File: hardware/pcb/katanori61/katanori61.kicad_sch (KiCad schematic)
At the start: 53 parts, among them J1 XIAO RISER, J10 BAT (JST-PH), J13 USB-C, J2 OLED, J4 SPK IN, J5 SPK OUT, J6 BTN2, J7 REED+TOGGLE, K31 G6S-2F DC5, Q1 MMUN2133LT1G, Q31 SS8050, U1 TPS61090RSAR, U2 MCP73871-2CCI/ML, U3 INA226AIDGSR, U4 AS5600-ASOM

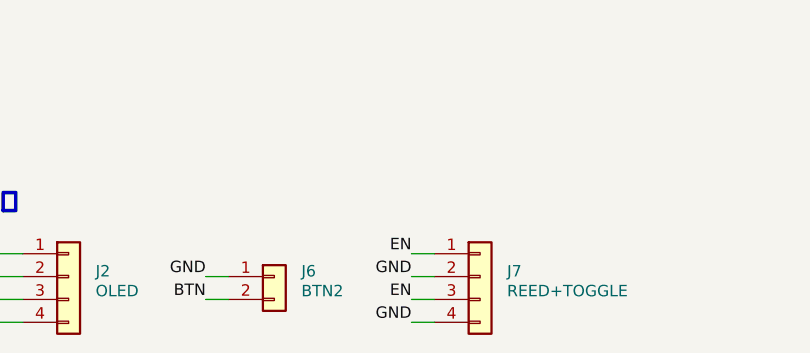
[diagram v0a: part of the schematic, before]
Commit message: 会話ボタンの口（J6）を板から外す（🔒 ユーザー 2026-09-14）
口は 4 つ（スピーカー IN・OUT・リード＋トグル・電池）になった。配線し直して
DRC のエラー 0・未接続 0。ガーバーと部品表も出し直した（実装は 29 種類 46 個で変わらず、
自分で付けるのが 7 → 6 個）。

⚠ BTN（XIAO の D2）は板の上では J1 の 6 番だけになった。会話ボタンの行き先は未決。
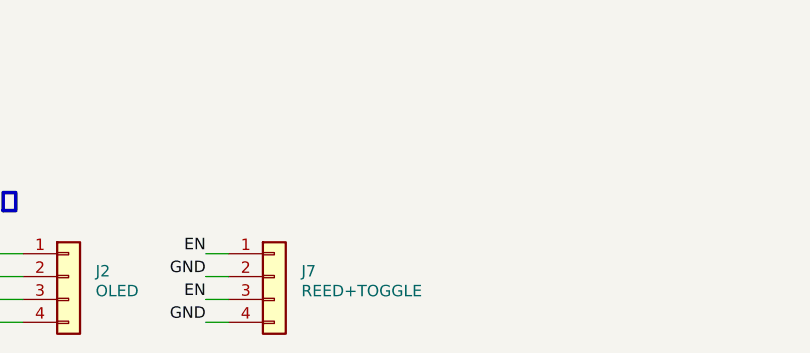
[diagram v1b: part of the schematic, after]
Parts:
- removed J7: REED+TOGGLE, Connector_JST:JST_PH_B4B-PH-K_1x04_P2.00mm_Vertical, symbol Connector_Generic:Conn_01x04
- J7: renamed from J6; value BTN2 -> REED+TOGGLE; footprint Connector_JST:JST_PH_S2B-PH-K_1x02_P2.00mm_Horizontal -> Connector_JST:JST_PH_B4B-PH-K_1x04_P2.00mm_Vertical; symbol Connector_Generic:Conn_01x02 -> Connector_Generic:Conn_01x04; Note 筐体の会話ボタンへ 2 本 -> 1 EN・2 GND → リード ／ 3 EN・4 GND → マスタートグル（縦の口・上から挿す）
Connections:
- net BTN: no longer J7.2 (Pin_2)
- net EN: now also J7.1 (Pin_1), J7.3 (Pin_3)
- net GND: now also J7.2 (Pin_2), J7.4 (Pin_4); no longer J7.1 (Pin_1)
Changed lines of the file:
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@@
 	)
 	(symbol
-		(lib_id "Connector_Generic:Conn_01x02")
+		(lib_id "Connector_Generic:Conn_01x04")
 		(at 109.22 243.84 0)
 		(unit 1)
@@
 		(on_board yes)
 		(dnp no)
-		(property "Reference" "J6"
+		(property "Reference" "J7"
 			(at 112.22 243.24 0)
 			(effects
@@
 			)
 		)
-		(property "Value" "BTN2"
+		(property "Value" "REED+TOGGLE"
 			(at 112.22 245.44 0)
 			(effects
@@
 			)
 		)
-		(property "Footprint" "Connector_JST:JST_PH_S2B-PH-K_1x02_P2.00mm_Horizontal"
+		(property "Footprint" "Connector_JST:JST_PH_B4B-PH-K_1x04_P2.00mm_Vertical"
 			(at 109.22 243.84 0)
 			(effects
@@
 			)
 		)
-		(property "Note" "筐体の会話ボタンへ 2 本"
+		(property "Note" "1 EN・2 GND → リード ／ 3 EN・4 GND → マスタートグル（縦の口・上から挿す）"
 			(at 109.22 243.84 0)
 			(effects
@@
 		(pin "2"
 		)
+		(pin "3"
+		)
+		(pin "4"
+		)
 		(instances
 			(project "katanori61"
 				(path "/377120ba-3fb3-530c-9f35-c36cf0274025"
-					(reference "J6")
+					(reference "J7")
 					(unit 1)
 				)
 			)
+		)
+	)
+	(wire
+		(pts
+			(xy 104.14 241.30)
+			(xy 101.60 241.30)
+		)
+		(stroke
+			(width 0)
+			(type default)
+		)
+	)
+	(label "EN"
+		(at 101.60 241.30 180)
+		(effects
+			(font
+				(size 1.27 1.27)
+			)
+			(justify right bottom)
 		)
 	)
@@
 		)
 	)
-	(label "BTN"
+	(label "EN"
 		(at 101.60 246.38 180)
-		(effects
-			(font
-				(size 1.27 1.27)
-			)
-			(justify right bottom)
-		)
-	)
-	(symbol
-		(lib_id "Connector_Generic:Conn_01x04")
-		(at 132.08 243.84 0)
-		(unit 1)
-		(exclude_from_sim no)
-		(in_bom yes)
-		(on_board yes)
-		(dnp no)
-		(property "Reference" "J7"
-			(at 135.08 243.24 0)
-			(effects
-				(font
-					(size 1.27 1.27)
-				)
-				(justify left)
-			)
-		)
-		(property "Value" "REED+TOGGLE"
-			(at 135.08 245.44 0)
-			(effects
-				(font
-					(size 1.27 1.27)
-				)
-				(justify left)
-			)
-		)
-		(property "Footprint" "Connector_JST:JST_PH_B4B-PH-K_1x04_P2.00mm_Vertical"
-			(at 132.08 243.84 0)
-			(effects
-				(font
-					(size 1.27 1.27)
-				)
-				(hide yes)
-			)
-		)
-		(property "Datasheet" ""
-			(at 132.08 243.84 0)
-			(effects
-				(font
-					(size 1.27 1.27)
-				)
-				(hide yes)
-			)
-		)
-		(property "Note" "1 EN・2 GND → リード ／ 3 EN・4 GND → マスタートグル（縦の口・上から挿す）"
-			(at 132.08 243.84 0)
-			(effects
-				(font
-					(size 1.27 1.27)
-				)
-				(hide yes)
-			)
-		)
-		(pin "1"
-		)
-		(pin "2"
-		)
-		(pin "3"
-		)
-		(pin "4"
-		)
-		(instances
-			(project "katanori61"
-				(path "/377120ba-3fb3-530c-9f35-c36cf0274025"
-					(reference "J7")
-					(unit 1)
-				)
-			)
-		)
-	)
-	(wire
-		(pts
-			(xy 127.00 241.30)
-			(xy 124.46 241.30)
-		)
-		(stroke
-			(width 0)
-			(type default)
-		)
-	)
-	(label "EN"
-		(at 124.46 241.30 180)
 		(effects
 			(font
@@
 	(wire
 		(pts
-			(xy 127.00 243.84)
-			(xy 124.46 243.84)
+			(xy 104.14 248.92)
+			(xy 101.60 248.92)
 		)
 		(stroke
@@
 	)
 	(label "GND"
-		(at 124.46 243.84 180)
+		(at 101.60 248.92 180)
 		(effects
 			(font
-				(size 1.27 1.27)
-			)
-			(justify right bottom)
-		)
-	)
-	(wire
-		(pts
-			(xy 127.00 246.38)
-			(xy 124.46 246.38)
-		)
-		(stroke
-			(width 0)
-			(type default)
-		)
-	)
-	(label "EN"
-		(at 124.46 246.38 180)
-		(effects
-			(font
-				(size 1.27 1.27)
-			)
-			(justify right bottom)
-		)
-	)
-	(wire
-		(pts
-			(xy 127.00 248.92)
-			(xy 124.46 248.92)
-		)
-		(stroke
-			(width 0)
-			(type default)
-		)
-	)
-	(label "GND"
-		(at 124.46 248.92 180)
-		(effects
-			(font

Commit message: 会話ボタンの口（J6）を戻す（外したのは伝言の読み違い）
🔒 ユーザー 2026-09-14「会話ボタンを基板に付ける必要はないと言ったんであって、線は必要でしょ。
天板の会話ボタンはあるんだし」＝ 押しボタンを板に載せないだけで、線を受ける口は要る。

枠も向きも外す前と同じ（板の座標 X 14.05〜20.95・Y 22.70〜31.30・口は −Y）。
板の部品 53・線が出る口 5 つ・自分で付ける 7 個に戻った。DRC のエラー 0・未接続 0。
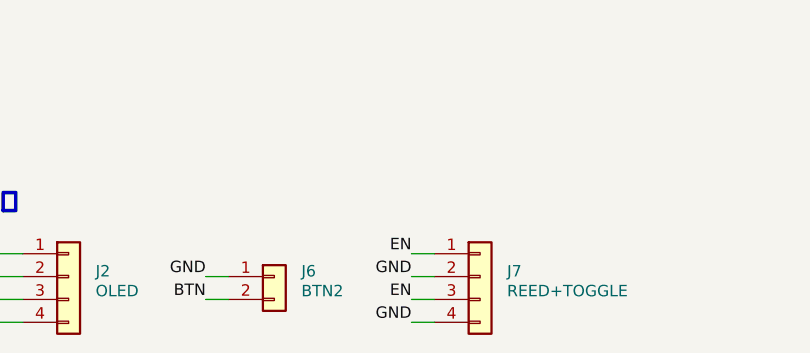
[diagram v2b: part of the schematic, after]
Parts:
- added J7: REED+TOGGLE, Connector_JST:JST_PH_B4B-PH-K_1x04_P2.00mm_Vertical, symbol Connector_Generic:Conn_01x04
- J6: renamed from J7; value REED+TOGGLE -> BTN2; footprint Connector_JST:JST_PH_B4B-PH-K_1x04_P2.00mm_Vertical -> Connector_JST:JST_PH_S2B-PH-K_1x02_P2.00mm_Horizontal; symbol Connector_Generic:Conn_01x04 -> Connector_Generic:Conn_01x02; Note 1 EN・2 GND → リード ／ 3 EN・4 GND → マスタートグル（縦の口・上から挿す） -> 天板の会話ボタンへ 2 本
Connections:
- net BTN: now also J6.2 (Pin_2)
- net EN: now also J7.1 (Pin_1), J7.3 (Pin_3); no longer J6.1 (Pin_1), J6.3 (Pin_3)
- net GND: now also J6.1 (Pin_1), J7.2 (Pin_2), J7.4 (Pin_4); no longer J6.2 (Pin_2), J6.4 (Pin_4)
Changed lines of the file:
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@@
 	)
 	(symbol
-		(lib_id "Connector_Generic:Conn_01x04")
+		(lib_id "Connector_Generic:Conn_01x02")
 		(at 109.22 243.84 0)
 		(unit 1)
@@
 		(on_board yes)
 		(dnp no)
-		(property "Reference" "J7"
+		(property "Reference" "J6"
 			(at 112.22 243.24 0)
 			(effects
@@
 			)
 		)
-		(property "Value" "REED+TOGGLE"
+		(property "Value" "BTN2"
 			(at 112.22 245.44 0)
 			(effects
@@
 			)
 		)
-		(property "Footprint" "Connector_JST:JST_PH_B4B-PH-K_1x04_P2.00mm_Vertical"
+		(property "Footprint" "Connector_JST:JST_PH_S2B-PH-K_1x02_P2.00mm_Horizontal"
 			(at 109.22 243.84 0)
 			(effects
@@
 			)
 		)
+		(property "Note" "天板の会話ボタンへ 2 本"
+			(at 109.22 243.84 0)
+			(effects
+				(font
+					(size 1.27 1.27)
+				)
+				(hide yes)
+			)
+		)
+		(pin "1"
+		)
+		(pin "2"
+		)
+		(instances
+			(project "katanori61"
+				(path "/377120ba-3fb3-530c-9f35-c36cf0274025"
+					(reference "J6")
+					(unit 1)
+				)
+			)
+		)
+	)
+	(wire
+		(pts
+			(xy 104.14 243.84)
+			(xy 101.60 243.84)
+		)
+		(stroke
+			(width 0)
+			(type default)
+		)
+	)
+	(label "GND"
+		(at 101.60 243.84 180)
+		(effects
+			(font
+				(size 1.27 1.27)
+			)
+			(justify right bottom)
+		)
+	)
+	(wire
+		(pts
+			(xy 104.14 246.38)
+			(xy 101.60 246.38)
+		)
+		(stroke
+			(width 0)
+			(type default)
+		)
+	)
+	(label "BTN"
+		(at 101.60 246.38 180)
+		(effects
+			(font
+				(size 1.27 1.27)
+			)
+			(justify right bottom)
+		)
+	)
+	(symbol
+		(lib_id "Connector_Generic:Conn_01x04")
+		(at 132.08 243.84 0)
+		(unit 1)
+		(exclude_from_sim no)
+		(in_bom yes)
+		(on_board yes)
+		(dnp no)
+		(property "Reference" "J7"
+			(at 135.08 243.24 0)
+			(effects
+				(font
+					(size 1.27 1.27)
+				)
+				(justify left)
+			)
+		)
+		(property "Value" "REED+TOGGLE"
+			(at 135.08 245.44 0)
+			(effects
+				(font
+					(size 1.27 1.27)
+				)
+				(justify left)
+			)
+		)
+		(property "Footprint" "Connector_JST:JST_PH_B4B-PH-K_1x04_P2.00mm_Vertical"
+			(at 132.08 243.84 0)
+			(effects
+				(font
+					(size 1.27 1.27)
+				)
+				(hide yes)
+			)
+		)
+		(property "Datasheet" ""
+			(at 132.08 243.84 0)
+			(effects
+				(font
+					(size 1.27 1.27)
+				)
+				(hide yes)
+			)
+		)
 		(property "Note" "1 EN・2 GND → リード ／ 3 EN・4 GND → マスタートグル（縦の口・上から挿す）"
-			(at 109.22 243.84 0)
+			(at 132.08 243.84 0)
 			(effects
 				(font
@@
 	(wire
 		(pts
-			(xy 104.14 241.30)
-			(xy 101.60 241.30)
+			(xy 127.00 241.30)
+			(xy 124.46 241.30)
 		)
 		(stroke
@@
 	)
 	(label "EN"
-		(at 101.60 241.30 180)
-		(effects
-			(font
-				(size 1.27 1.27)
-			)
-			(justify right bottom)
-		)
-	)
-	(wire
-		(pts
-			(xy 104.14 243.84)
-			(xy 101.60 243.84)
+		(at 124.46 241.30 180)
+		(effects
+			(font
+				(size 1.27 1.27)
+			)
+			(justify right bottom)
+		)
+	)
+	(wire
+		(pts
+			(xy 127.00 243.84)
+			(xy 124.46 243.84)
 		)
 		(stroke
@@
 	)
 	(label "GND"
-		(at 101.60 243.84 180)
-		(effects
-			(font
-				(size 1.27 1.27)
-			)
-			(justify right bottom)
-		)
-	)
-	(wire
-		(pts
-			(xy 104.14 246.38)
-			(xy 101.60 246.38)
+		(at 124.46 243.84 180)
+		(effects
+			(font
+				(size 1.27 1.27)
+			)
+			(justify right bottom)
+		)
+	)
+	(wire
+		(pts
+			(xy 127.00 246.38)
+			(xy 124.46 246.38)
 		)
 		(stroke
@@
 	)
 	(label "EN"
-		(at 101.60 246.38 180)
-		(effects
-			(font
-				(size 1.27 1.27)
-			)
-			(justify right bottom)
-		)
-	)
-	(wire
-		(pts
-			(xy 104.14 248.92)
-			(xy 101.60 248.92)
+		(at 124.46 246.38 180)
+		(effects
+			(font
+				(size 1.27 1.27)
+			)
+			(justify right bottom)
+		)
+	)
+	(wire
+		(pts
+			(xy 127.00 248.92)
+			(xy 124.46 248.92)
 		)
 		(stroke
@@
 	)
 	(label "GND"
-		(at 101.60 248.92 180)
-		(effects
-			(font
+		(at 124.46 248.92 180)
+		(effects
+			(font

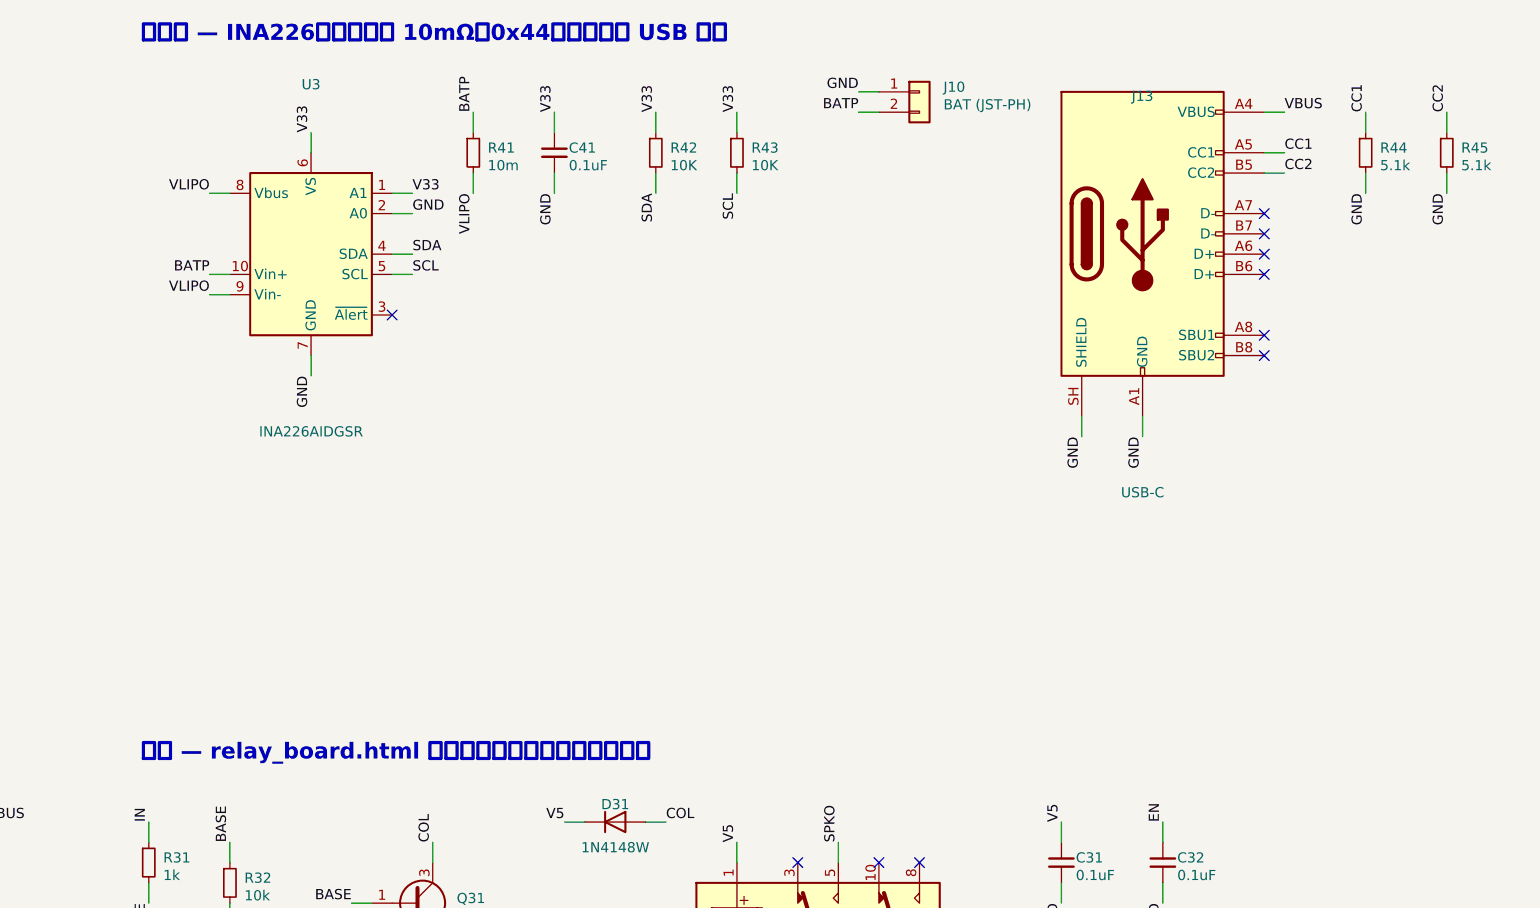
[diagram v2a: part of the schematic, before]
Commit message: pcb v6.1: J10 を縦の B2B-PH-K へ・逆接保護の MOSFET を追加・取付穴の移動と欠きの全廃に追随
筐体側の 2026-09-16 夕の作り替え（電池のケーシング・床から立つ左後ろの柱）に合わせて、
基板を出し直した。DRC エラー 0・未接続 0・回路図との食い違い 0。

■ J10（電池の口）を縦へ
🔒 ユーザー「ケーシング作ったから垂直のがいい。結局一番穴は小さくなる」。
サイド型 S2B-PH-K（背 4.8・横出し）→ トップ型 B2B-PH-K を板の裏に下向き。左の帯 → 右の帯。
・天板の窓が 12.7 × 7.9（100.3mm2）→ 8.11 × 5.91（47.9mm2）。挿しても平面の外形が広がらない
  （ハウジング PHR-2 5.8 × 4.5 が胴 5.9 × 4.5 の中に収まる。ePH.pdf 3 ページ）
・J10 は板の裏でも、はんだ足 2 本は表へ突き抜ける。その足を J4 の胴（板 y 〜14.30）と
  J4 に挿さったプラグ（〜16.30）の外へ出す必要があり、USB-C のシェルの足（20.63〜）との
  あいだが 4.33 しか無いのでパッドを Y 並び → X 並びへ回した
・その結果、極性の言い方が「手前／奥」から「左／右」へ変わった（右 77.45 が GND・左 75.45 が VBAT+）。
  ネットの割り当て（1 番 = GND・2 番 = +）は変えていない

■ 逆接保護の P-ch MOSFET（Q2）
🔒 ユーザー「MOSFET 一つ入れましょ」。J10 の 2 番とシャント R41 のあいだへ。
・AO3401A（LCSC C15127・JLCPCB Basic・Vgs(th) 900mV・RDS(on) 60mΩ@4.5V / 85mΩ@2.5V）
  ＋ ゲートの 100kΩ（R46 は R17 と同じ品なので部品の種類は増えない）
・ドレイン(3) = 電池側 BATRAW / ソース(2) = 負荷側 BATP / ゲート(1) = 100kΩ で GND。
  逆に繋ぐとボディダイオードが逆方向・Vgs = 0 でチャネルも閉じたまま → 電流が流れない
・保護の外に残るのは BATRAW の線と Q2 のドレインだけ。2026-09-11 に焼けた INA226 は
  入力も電源も内側にある。逆接の症状は「何も起きない」になる
・J10 の横は J4 のプラグの逃げと USB-C に挟まれて 2.78 しか無く SOT-23 が入らないので
  シャントの隣に置いた。電池の電流はもともと板を横断しているので経路は伸びない

■ 筐体の作り替えへの追随
・取付穴 4 点: (4.0, 3.5) (72.5, 3.5) (2.834, 33.9942) (79.354, 34.9)。4 点とも使う
  （上から 3 本・下から 1 本）。旧の後ろ 2 点 (10.0, 33.4) (72.5, 33.4) から移動
・板の欠きを全廃。残るのは後ろのレールの逃げ（板 X 0〜1.694・Y 37.1〜37.4）だけ。
  幅はレール 1.2 + 板を右へ 0.8 滑らせる分。銅が 41mm2 戻った
・板の裏は両材料とも Z 12.0（BAT_CASE 6.0 がレジンにも入った）

■ 検査の道具の直し（どれも見落としを実際に出したもの）
・gen_pcb: 枠の重なりを面ごとに。表と裏を 1 枚の紙として見ていて、板を挟んで別の側に居る物を
  重なりと呼んでいた。別の面どうしは「板を貫く足が相手の胴に入っていないか」で見る
・gen_pcb: courtyard() に key="Fab" を足した。courtyard は置き場所の予約で物の形ではない
・gen_pcb: プラグの通り道の検査が、裏の部品の足を見ていなかった。J10 の足が J4 のプラグの
  真下に入るのを筐体側の hit_wires が先に見つけた
・gen_pcb: 押し離しも面ごとに（表と裏で押し合って収束しなかった）
・gen_pcb: PLUG_BODY 3.1 → 1.5。3.1 は導出が間違っていた（SMT の図の (9.6) から
  トップ型の背 6.0 を引いていた。正はサイド型の奥行き 7.6 を引いて 2.0 = courtyard から 1.5）
  押し離しの予約だけは 3.1 のまま（PLUG_KEEP・置き方の手加減で検査の値ではない）
・route.py --incremental: 「φ0.59 以上は縫いのビア」として自動配線のビア（φ0.8）まで
  種から落としていた。多層をまたぐネットが切れて未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
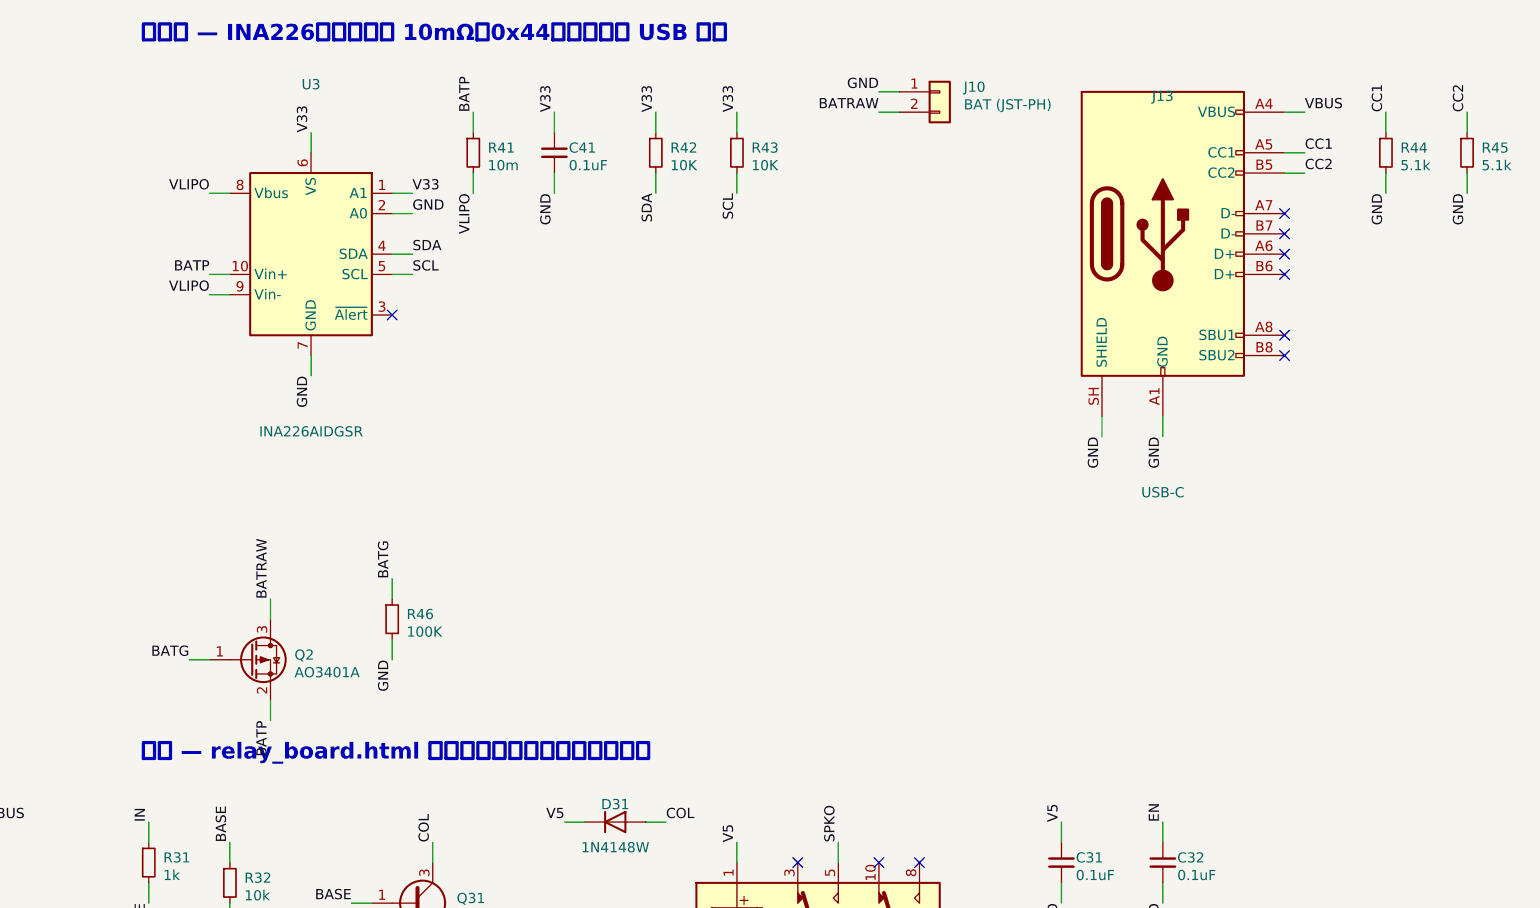
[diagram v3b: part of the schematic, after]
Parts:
- removed Q31: SS8050, Package_TO_SOT_SMD:SOT-23, symbol Transistor_BJT:MMBT3904
- removed R32: 10k, Resistor_SMD:R_0805_2012Metric, symbol Device:R_Small
- added D31: 1N4148W, Diode_SMD:D_SOD-123, symbol Diode:1N4148W
- added K31: G6S-2F DC5, Relay_SMD:Relay_DPDT_Omron_G6S-2F, symbol Relay:G6S-2
- added R31: 1k, Resistor_SMD:R_0805_2012Metric, symbol Device:R_Small
- added R46: 100K, Resistor_SMD:R_0805_2012Metric, symbol Device:R_Small
- J10: footprint Connector_JST:JST_PH_S2B-PH-K_1x02_P2.00mm_Horizontal -> Connector_JST:JST_PH_B2B-PH-K_1x02_P2.00mm_Vertical; Note 🔴 1 番が −・2 番が +（PowerBoost B1 の並び）。v6.1 は板の裏に横出し（🔒 ユーザー 202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 -> 🔴 1 番が −・2 番が ＋（PowerBoost B1 の並び。⭐ 2026-09-16 夕から 2 番のネットは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
- Q2: renamed from R31; value 1k -> AO3401A; footprint Resistor_SMD:R_0805_2012Metric -> Package_TO_SOT_SMD:SOT-23; symbol Device:R_Small -> Transistor_FET:Q_PMOS_GSD; LCSC C17513 -> C15127; Note relay_board R1 -> 逆接保護（P-ch）。1=G・2=S・3=D は AO3401A の SOT-23 の並び。📄 LCSC C15127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
- Q31: renamed from K31; value G6S-2F DC5 -> SS8050; footprint Relay_SMD:Relay_DPDT_Omron_G6S-2F -> Package_TO_SOT_SMD:SOT-23; symbol Relay:G6S-2 -> Transistor_BJT:MMBT3904; LCSC C16707 -> C2150; Note COM–NO を使う・NC は空き。2 回路のうち使うのは 1 回路だけ（もう 1 回路は未接続） -> relay_board Q1（2SC1815-GR の表面実装の代わり・SOT-23 は 1=B・2=E・3=C）
- R32: renamed from D31; value 1N4148W -> 10k; footprint Diode_SMD:D_SOD-123 -> Resistor_SMD:R_0805_2012Metric; symbol Diode:1N4148W -> Device:R_Small; LCSC C81598 -> C17414; Note relay_board D1・カソードが +5V（表面実装の 1N4148W） -> relay_board R2・🔴 安全の要
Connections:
- net BASE: now also Q31.1 (B), R32.1, R31.2; no longer Q2.2
- net BATP: now also Q2.2 (S); no longer J10.2 (Pin_2)
- net COL: now also Q31.3 (C), D31.2 (A), K31.12; no longer Q31.12, R32.2 (A)
- net GND: now also Q31.2 (E), R32.2, R46.2
- net IN: now also R31.1; no longer Q2.1
- net SPKO: now also K31.5; no longer Q31.5
- net SPKP: now also K31.4; no longer Q31.4
- net V5: now also D31.1 (K), K31.1; no longer Q31.1, R32.1 (K)
- new net BATG: Q2.1 (G), R46.1
- new net BATRAW: J10.2 (Pin_2), Q2.3 (D)
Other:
- moved on the sheet: J10, J13, R44, R45
